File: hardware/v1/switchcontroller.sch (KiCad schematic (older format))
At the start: 1 part

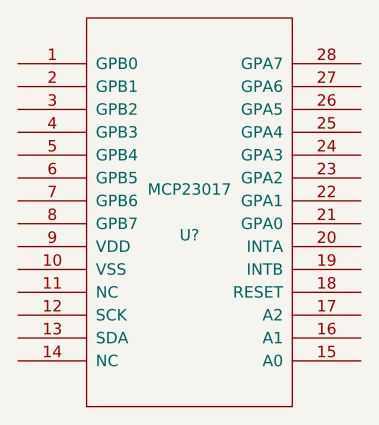
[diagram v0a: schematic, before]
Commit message: Some autorouting on 16led row
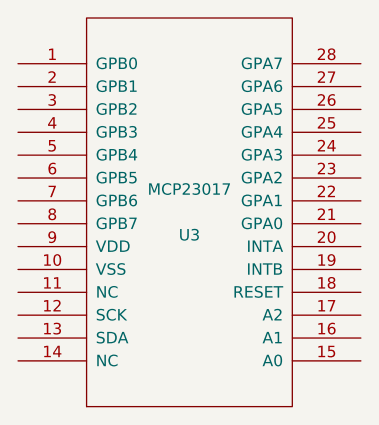
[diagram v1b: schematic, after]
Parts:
- U3: renamed from U?; footprint MODULE -> DIL28:DIL28
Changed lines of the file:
@@
 $EndDescr
 $Comp
-L MCP23017 U?
+L MCP23017 U3
 U 1 1 57A3D3D3
 P 4900 3000
-F 0 "U?" H 4900 2900 50  0000 C CNN
+F 0 "U3" H 4900 2900 50  0000 C CNN
 F 1 "MCP23017" H 4900 3100 50  0000 C CNN
-F 2 "MODULE" H 4900 3000 50  0001 C CNN
+F 2 "DIL28:DIL28" H 4900 3000 50  0001 C CNN
 F 3 "DOCUMENTATION" H 4900 3000 50  0001 C CNN
 	1    4900 3000
